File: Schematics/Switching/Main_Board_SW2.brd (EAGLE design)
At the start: 100 x 80 mm, 83 parts, among them IC3 SWITCHER, IC4 SWITCHER, Q1 32.768kHz, X1 MINI-USB-SHIELD-UX60-MB-5ST, X2 RJ45

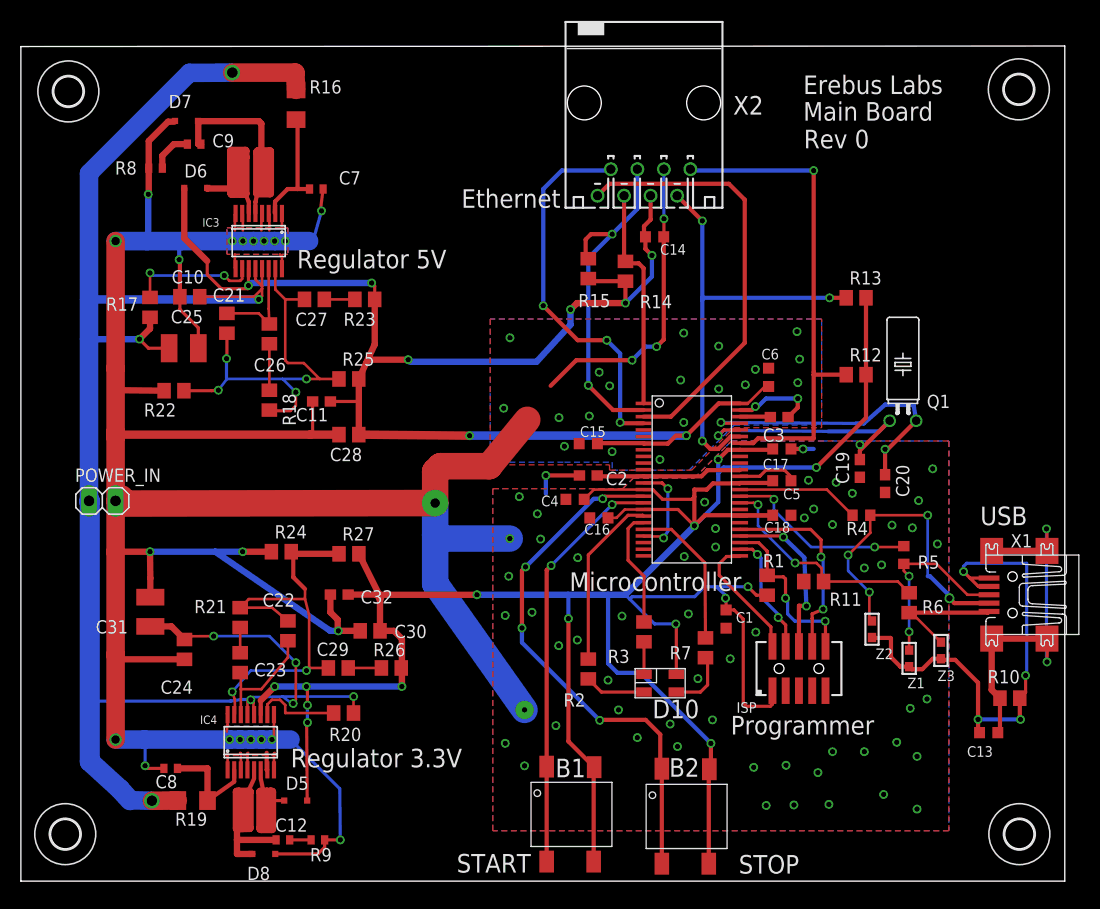
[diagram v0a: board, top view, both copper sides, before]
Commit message: Updated Switcher Board
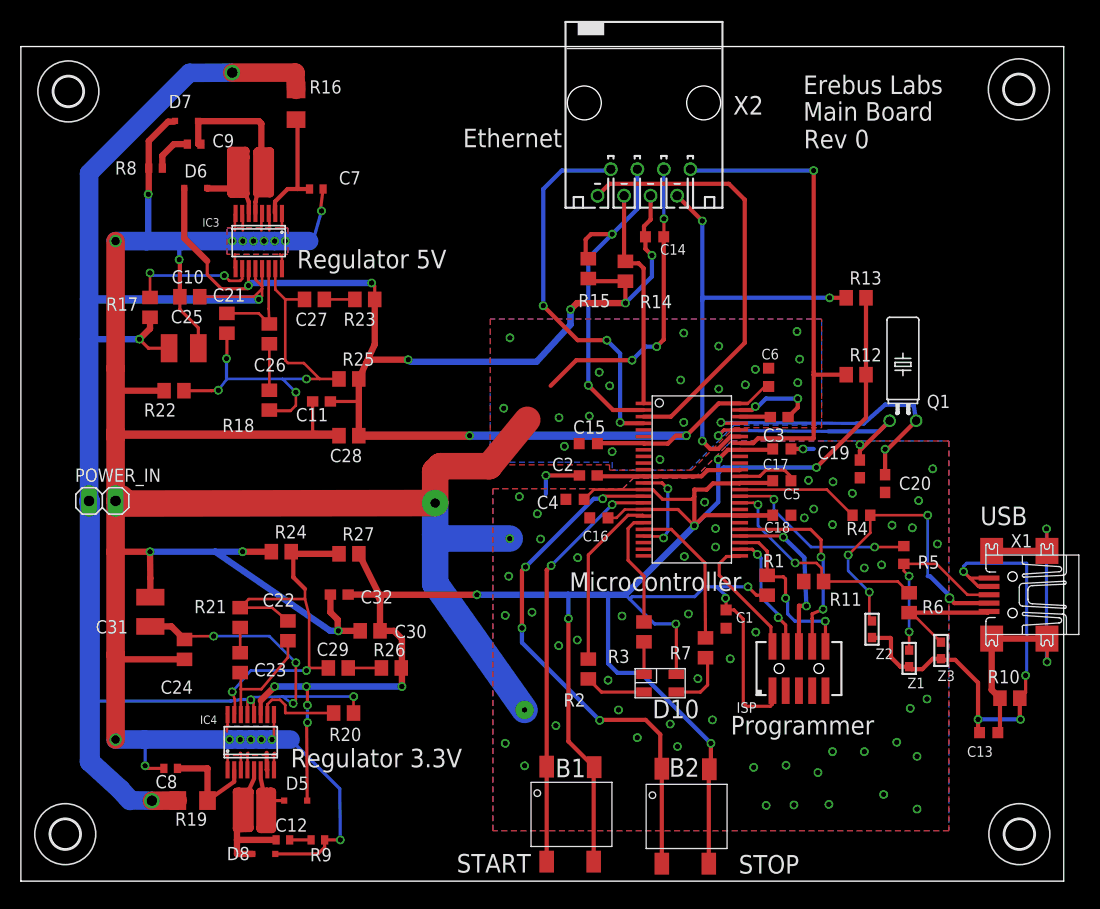
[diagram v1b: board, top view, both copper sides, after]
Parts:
- moved C28 0.10 mm to (31.4, 42.7)
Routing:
- net GND: track 427.9 -> 429.9 mm
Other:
- board size 100 x 80 mm -> 99.9 x 80 mm
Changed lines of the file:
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@@
 <?xml version="1.0" encoding="utf-8"?>
 <!DOCTYPE eagle SYSTEM "eagle.dtd">
-<eagle version="6.5.0">
+<eagle version="6.3">
 <drawing>
 <settings>
@@
 <setting verticaltext="up"/>
 </settings>
-<grid distance="0.05" unitdist="mm" unit="mm" style="lines" multiple="1" display="yes" altdistance="0.025" altunitdist="inch" altunit="inch"/>
+<grid distance="0.025" unitdist="mm" unit="mm" style="lines" multiple="1" display="yes" altdistance="0.025" altunitdist="mm" altunit="mm"/>
 <layers>
 <layer number="1" name="Top" color="4" fill="1" visible="yes" active="yes"/>
@@
 <layer number="25" name="tNames" color="7" fill="1" visible="yes" active="yes"/>
 <layer number="26" name="bNames" color="7" fill="1" visible="yes" active="yes"/>
-<layer number="27" name="tValues" color="7" fill="1" visible="no" active="yes"/>
-<layer number="28" name="bValues" color="7" fill="1" visible="no" active="yes"/>
+<layer number="27" name="tValues" color="7" fill="1" visible="yes" active="yes"/>
+<layer number="28" name="bValues" color="7" fill="1" visible="yes" active="yes"/>
 <layer number="29" name="tStop" color="7" fill="3" visible="yes" active="yes"/>
 <layer number="30" name="bStop" color="7" fill="6" visible="yes" active="yes"/>
@@
 <board>
 <plain>
-<wire x1="0" y1="0" x2="100" y2="0" width="0" layer="20"/>
-<wire x1="100" y1="0" x2="100" y2="80" width="0" layer="20"/>
-<wire x1="100" y1="80" x2="0" y2="79.95" width="0" layer="20"/>
+<wire x1="0" y1="0" x2="99.9" y2="0" width="0" layer="20"/>
+<wire x1="99.9" y1="0" x2="99.9" y2="79.95" width="0" layer="20"/>
+<wire x1="99.9" y1="79.95" x2="0" y2="79.95" width="0" layer="20"/>
 <wire x1="0" y1="79.95" x2="0" y2="0" width="0" layer="20"/>
 <text x="60.5" y="15.6" size="1.778" layer="25">D10</text>
@@
 </polygon>
 <text x="91.9" y="34.1" size="1.778" layer="25">USB</text>
-<text x="42.2" y="64.5" size="1.778" layer="25">Ethernet</text>
+<text x="42.35" y="70.3" size="1.778" layer="25">Ethernet</text>
 <text x="52.55" y="27.8" size="1.778" layer="25">Microcontroller</text>
 <text x="68" y="14.05" size="1.778" layer="25">Programmer</text>
@@
 </element>
 <element name="C2" library="rcl" package="C0603" value="1uF" x="54.356" y="38.862" smashed="yes">
-<attribute name="NAME" x="58.129" y="39.203" size="1.27" layer="25" rot="R180"/>
+<attribute name="NAME" x="52.979" y="40.553" size="1.27" layer="25" rot="R180"/>
 <attribute name="VALUE" x="53.721" y="36.957" size="1.27" layer="27"/>
 </element>
@@
 </element>
 <element name="C4" library="rcl" package="C0603K" value="0.1uF" x="53.086" y="36.576" smashed="yes">
-<attribute name="NAME" x="51.514" y="36.924" size="1.016" layer="25" rot="R180"/>
+<attribute name="NAME" x="51.514" y="36.924" size="1.27" layer="25" rot="R180"/>
 <attribute name="VALUE" x="52.286" y="34.926" size="1.016" layer="27"/>
 </element>
@@
 </element>
 <element name="C15" library="rcl" package="C0603K" value="0.1uF" x="54.356" y="41.91" smashed="yes">
-<attribute name="NAME" x="53.556" y="42.56" size="1.016" layer="25"/>
+<attribute name="NAME" x="52.906" y="42.86" size="1.27" layer="25"/>
 <attribute name="VALUE" x="53.556" y="40.26" size="1.016" layer="27"/>
 </element>
 <element name="C16" library="rcl" package="C0603K" value="0.1uF" x="55.372" y="34.798" smashed="yes">
-<attribute name="NAME" x="53.972" y="33.198" size="1.016" layer="25"/>
+<attribute name="NAME" x="53.822" y="32.548" size="1.016" layer="25"/>
 <attribute name="VALUE" x="54.572" y="33.148" size="1.016" layer="27"/>
 </element>
@@
 <attribute name="VALUE" x="87.671" y="46.136" size="1.27" layer="27" ratio="10" rot="R90"/>
 </element>
-<element name="C19" library="rcl" package="C0603" value="22pF" x="80.37" y="39.538" smashed="yes" rot="R90">
-<attribute name="NAME" x="79.335" y="38.053" size="1.27" layer="25" rot="R90"/>
-<attribute name="VALUE" x="82.275" y="38.903" size="1.27" layer="27" rot="R90"/>
+<element name="C19" library="rcl" package="C0603" value="22pF" x="80.37" y="39.488" smashed="yes" rot="R90">
+<attribute name="NAME" x="79.397" y="41.685" size="1.27" layer="25" rot="R180"/>
+<attribute name="VALUE" x="82.275" y="38.853" size="1.27" layer="27" rot="R90"/>
 </element>
 <element name="C20" library="rcl" package="C0603" value="22pF" x="82.788" y="38.084" smashed="yes" rot="R90">
-<attribute name="NAME" x="85.103" y="36.799" size="1.27" layer="25" rot="R90"/>
+<attribute name="NAME" x="87.201" y="38.753" size="1.27" layer="25" rot="R180"/>
 <attribute name="VALUE" x="84.693" y="37.449" size="1.27" layer="27" rot="R90"/>
 </element>
@@
 </element>
 <element name="R18" library="rcl" package="R0805" value="15k" x="23.802" y="46.074" smashed="yes" rot="R270">
-<attribute name="NAME" x="25.072" y="46.709" size="1.27" layer="25" rot="R270"/>
+<attribute name="NAME" x="19.291" y="43.022" size="1.27" layer="25"/>
 <attribute name="VALUE" x="21.262" y="46.709" size="1.27" layer="27" rot="R270"/>
 </element>
@@
 <attribute name="VALUE" x="29.39" y="58.266" size="1.27" layer="27" rot="R180"/>
 </element>
-<element name="C28" library="rcl" package="C0805" value="22uF" x="31.422" y="42.772" smashed="yes" rot="R180">
-<attribute name="NAME" x="32.692" y="41.502" size="1.27" layer="25" rot="R180"/>
-<attribute name="VALUE" x="32.692" y="45.312" size="1.27" layer="27" rot="R180"/>
+<element name="C28" library="rcl" package="C0805" value="22uF" x="31.422" y="42.672" smashed="yes" rot="R180">
+<attribute name="NAME" x="32.692" y="41.402" size="1.27" layer="25" rot="R180"/>
+<attribute name="VALUE" x="32.692" y="45.212" size="1.27" layer="27" rot="R180"/>
 </element>
 <element name="R25" library="rcl" package="R0805" value="649k" x="31.422" y="48.106" smashed="yes">
@@
 </element>
 <element name="D8" library="diode" package="SOD323-R" value="" x="23.27" y="2.606" smashed="yes">
-<attribute name="NAME" x="21.67" y="0.106" size="1.27" layer="25"/>
+<attribute name="NAME" x="19.72" y="2.006" size="1.27" layer="25"/>
 <attribute name="VALUE" x="22.17" y="0.306" size="1.27" layer="27"/>
 </element>
@@
 <wire x1="24.2465" y1="15.9538" x2="24.2465" y2="13.7525" width="0.254" layer="1"/>
 <wire x1="24.2465" y1="13.7525" x2="24.056" y2="13.562" width="0.254" layer="1"/>
-<wire x1="13.72" y1="46.98" x2="9.128" y2="47.03" width="0.6096" layer="1"/>
-<wire x1="9.128" y1="47.03" x2="9.07" y2="49.122" width="0.6096" layer="1"/>
+<wire x1="13.72" y1="46.98" x2="9.128" y2="46.98" width="0.6096" layer="1"/>
+<wire x1="9.128" y1="46.98" x2="9.07" y2="49.122" width="0.6096" layer="1"/>
 <wire x1="23.6115" y1="10.6622" x2="23.548" y2="10.6622" width="0.4064" layer="1"/>
 <wire x1="23.548" y1="10.6622" x2="23.548" y2="12.292" width="0.4064" layer="1"/>
@@
 <wire x1="44.868" y1="39.75" x2="48.514" y2="44.196" width="2.54" layer="1"/>
 <via x="46.832" y="32.816" extent="1-16" drill="0.5" diameter="0.254"/>
-<wire x1="30.472" y1="42.772" x2="27.7" y2="42.772" width="0.8128" layer="1"/>
-<wire x1="27.7" y1="42.772" x2="9.324" y2="42.772" width="0.8128" layer="1"/>
+<wire x1="30.472" y1="42.672" x2="30.3" y2="42.772" width="0.8128" layer="1"/>
+<wire x1="30.3" y1="42.772" x2="9.324" y2="42.772" width="0.8128" layer="1"/>
 <wire x1="9.324" y1="42.772" x2="9.07" y2="42.518" width="0.8128" layer="1"/>
 <wire x1="39.686" y1="36.218" x2="39.686" y2="33.17" width="2.54" layer="16"/>
@@
 <via x="87.35" y="39.5" extent="1-16" drill="0.5" diameter="0.254"/>
 <via x="79.65" y="37.15" extent="1-16" drill="0.5" diameter="0.254"/>
-<via x="78.1" y="38.2" extent="1-16" drill="0.5" diameter="0.254"/>
+<via x="77.8" y="38.25" extent="1-16" drill="0.5" diameter="0.254"/>
 <via x="65.5" y="36.3" extent="1-16" drill="0.5" diameter="0.254"/>
 <via x="66.548" y="33.782" extent="1-16" drill="0.5" diameter="0.254"/>
@@
 <wire x1="17" y1="53" x2="17" y2="51.05" width="0.3048" layer="1"/>
 <wire x1="27.95" y1="45.95" x2="27.95" y2="43.022" width="0.3048" layer="1"/>
-<wire x1="27.95" y1="43.022" x2="27.7" y2="42.772" width="0.3048" layer="1"/>
+<wire x1="27.95" y1="43.022" x2="30.3" y2="42.772" width="0.3048" layer="1"/>
 <wire x1="28.95" y1="66.3" x2="28.7" y2="64.3" width="0.3048" layer="1"/>
 <wire x1="28.7" y1="64.3" x2="28.8" y2="64.2" width="0.3048" layer="1"/>
@@
 <wire x1="33.896" y1="51.408" x2="33.896" y2="55.726" width="0.6096" layer="1"/>
 <wire x1="32.372" y1="48.106" x2="32.372" y2="46" width="0.6096" layer="1"/>
-<wire x1="32.372" y1="46" x2="32.372" y2="42.772" width="0.6096" layer="1"/>
+<wire x1="32.372" y1="46" x2="32.372" y2="42.672" width="0.6096" layer="1"/>
 <wire x1="59.65063125" y1="41.95445" x2="55.27545" y2="41.95445" width="0.4064" layer="1"/>
 <wire x1="55.27545" y1="41.95445" x2="55.231" y2="41.91" width="0.4064" layer="1"/>
-<wire x1="32.372" y1="42.772" x2="42.984" y2="42.672" width="0.8128" layer="1"/>
+<wire x1="32.372" y1="42.672" x2="42.984" y2="42.672" width="0.8128" layer="1"/>
 <via x="42.984" y="42.672" extent="1-16" drill="0.5" diameter="0.254"/>
 <wire x1="42.984" y1="42.672" x2="63.754" y2="42.672" width="0.8128" layer="16"/>
@@
 <via x="66.802" y="42.672" extent="1-16" drill="0.5" diameter="0.254"/>
 <via x="80.37" y="41.802" extent="1-16" drill="0.5" diameter="0.254"/>
-<wire x1="80.37" y1="41.802" x2="80.37" y2="40.388" width="0.3048" layer="1"/>
+<wire x1="80.37" y1="41.802" x2="80.37" y2="40.338" width="0.3048" layer="1"/>
 <wire x1="66.802" y1="42.672" x2="67.31" y2="43.18" width="0.3048" layer="16"/>
 <wire x1="67.31" y1="43.18" x2="77.342" y2="43.08" width="0.3048" layer="16"/>
-<wire x1="80.37" y1="40.388" x2="80.37" y2="41.248" width="0.4064" layer="1"/>
+<wire x1="80.37" y1="40.338" x2="80.37" y2="41.248" width="0.4064" layer="1"/>
 <wire x1="80.37" y1="41.248" x2="83.226" y2="44.104" width="0.4064" layer="1"/>
 <wire x1="77.342" y1="43.08" x2="82.202" y2="43.08" width="0.4064" layer="16"/>

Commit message: PCB Push
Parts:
- added R28, R29: 5.6k, rcl:R0805
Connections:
- new net N$22: R28.1, R29.2, U$1.P$44
- net GND: now also R29.1
- net V+: now also R28.2
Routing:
- net V+: track 187.5 -> 236.1 mm, vias 9 -> 10
- net N$22: track 0.00 -> 16.5 mm
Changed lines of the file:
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@@
 <element name="H3" library="holes" package="2,8" value="MOUNT-HOLE2.8" x="95.6" y="75.85"/>
 <element name="H4" library="holes" package="2,8" value="MOUNT-HOLE2.8" x="4.55" y="75.65"/>
+<element name="R28" library="rcl" package="R0805" value="5.6k" x="48.7" y="44" rot="R270"/>
+<element name="R29" library="rcl" package="R0805" value="5.6k" x="48.65" y="49.675" rot="R270"/>
 </elements>
 <signals>
@@
 <wire x1="12.2" y1="65.8" x2="12.2" y2="61.564" width="0.6096" layer="16"/>
 <wire x1="12.2" y1="61.564" x2="11.95" y2="61.314" width="0.6096" layer="16"/>
+<contactref element="R29" pad="1"/>
+<wire x1="61.214" y1="40.386" x2="61.42355" y2="38.14445" width="0" layer="19" extent="1-1"/>
 </signal>
 <signal name="N$11">
@@
 <contactref element="C24" pad="1"/>
 <contactref element="POWER_IN" pad="1"/>
-<wire x1="6.53" y1="36.422" x2="6.53" y2="51.916" width="1.778" layer="16"/>
+<wire x1="6.53" y1="36.422" x2="6.53" y2="39.725" width="1.778" layer="16"/>
+<wire x1="6.53" y1="39.725" x2="6.53" y2="40.3" width="1.778" layer="16"/>
+<wire x1="6.53" y1="40.3" x2="6.53" y2="51.916" width="1.778" layer="16"/>
 <wire x1="6.53" y1="51.916" x2="6.53" y2="55.726" width="1.778" layer="16"/>
 <wire x1="6.53" y1="55.726" x2="6.53" y2="67.808" width="1.778" layer="16"/>
@@
 <via x="20.25" y="77.45" extent="1-16" drill="1"/>
 <wire x1="20.25" y1="77.45" x2="26.3" y2="77.45" width="1.778" layer="1"/>
+<contactref element="R28" pad="2"/>
+<wire x1="48.7" y1="43.05" x2="46.225" y2="43.05" width="0.4064" layer="1"/>
+<wire x1="46.225" y1="43.05" x2="43.5" y2="45.775" width="0.4064" layer="1"/>
+<wire x1="43.5" y1="45.775" x2="36.925" y2="45.775" width="0.4064" layer="1"/>
+<wire x1="36.925" y1="45.775" x2="36.05" y2="44.9" width="0.4064" layer="1"/>
+<wire x1="7.005" y1="39.825" x2="6.53" y2="40.3" width="0.4064" layer="16"/>
+<via x="36.05" y="44.9" extent="1-16" drill="0.5" diameter="0.254" shape="octagon"/>
+<wire x1="36.05" y1="44.9" x2="36.05" y2="41.45" width="0.4064" layer="16"/>
+<wire x1="36.05" y1="41.45" x2="34.225" y2="39.625" width="0.4064" layer="16"/>
+<wire x1="34.225" y1="39.625" x2="6.63" y2="39.625" width="0.4064" layer="16"/>
+<wire x1="6.63" y1="39.625" x2="6.53" y2="39.725" width="0.4064" layer="16"/>
 </signal>
 <signal name="N$13">
@@
 </signal>
 <signal name="N$21">
-<via x="54.45" y="44.55" extent="1-16" drill="0.5" diameter="0.254"/>
+<via x="53.15" y="44.8" extent="1-16" drill="0.5" diameter="0.254"/>
 </signal>
 <signal name="N$90">
@@
 <wire x1="25.75" y1="3.95" x2="27.8" y2="3.95" width="0.3048" layer="1"/>
 </signal>
+<signal name="N$22">
+<contactref element="R29" pad="2"/>
+<contactref element="R28" pad="1"/>
+<wire x1="48.7" y1="44.95" x2="48.7" y2="46.475" width="0.4064" layer="1"/>
+<wire x1="48.7" y1="46.475" x2="48.7" y2="48.675" width="0.4064" layer="1"/>
+<wire x1="48.7" y1="48.675" x2="48.65" y2="48.725" width="0.4064" layer="1"/>
+<contactref element="U$1" pad="P$44"/>
+<wire x1="59.65063125" y1="43.22445" x2="58.47445" y2="43.22445" width="0.3048" layer="1"/>
+<wire x1="58.47445" y1="43.22445" x2="57.95" y2="42.7" width="0.3048" layer="1"/>
+<wire x1="57.95" y1="42.7" x2="56.925" y2="42.7" width="0.3048" layer="1"/>
+<wire x1="56.925" y1="42.7" x2="53.15" y2="46.475" width="0.3048" layer="1"/>
+<wire x1="53.15" y1="46.475" x2="48.7" y2="46.475" width="0.3048" layer="1"/>
+</signal>
 </signals>
